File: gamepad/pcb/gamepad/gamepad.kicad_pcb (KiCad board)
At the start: 2 copper layers, 67.8 x 67.8 mm, 10 parts, among them U1 Pico, U2 ADC

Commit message: feat: some pcb stuff
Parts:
- added U3: RP2040-ZERO, RP2040-ZERO:MODULE_RP2040-ZERO, F.Cu at (145.9, 70.3)

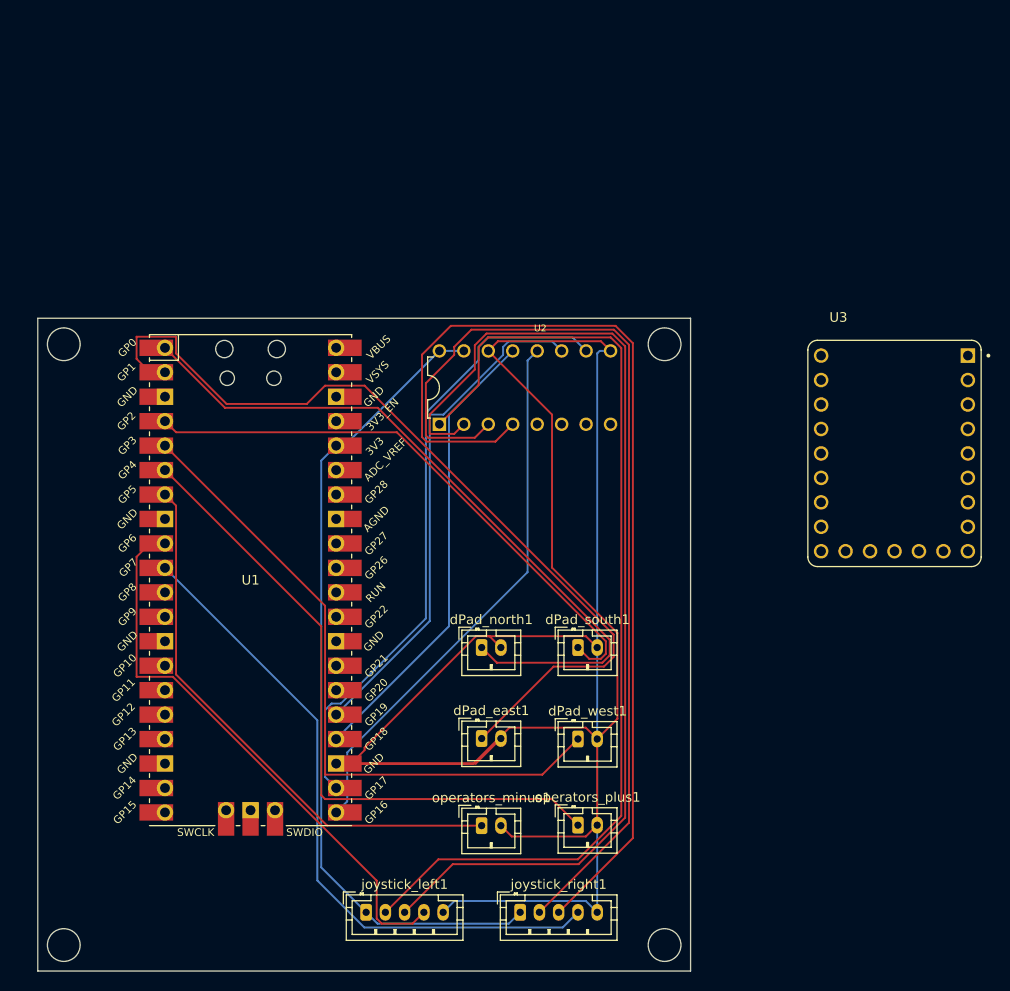
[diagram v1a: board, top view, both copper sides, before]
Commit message: upt: pico to waveshare zero
change out the pcb to have a waveshare zero instead of a pico
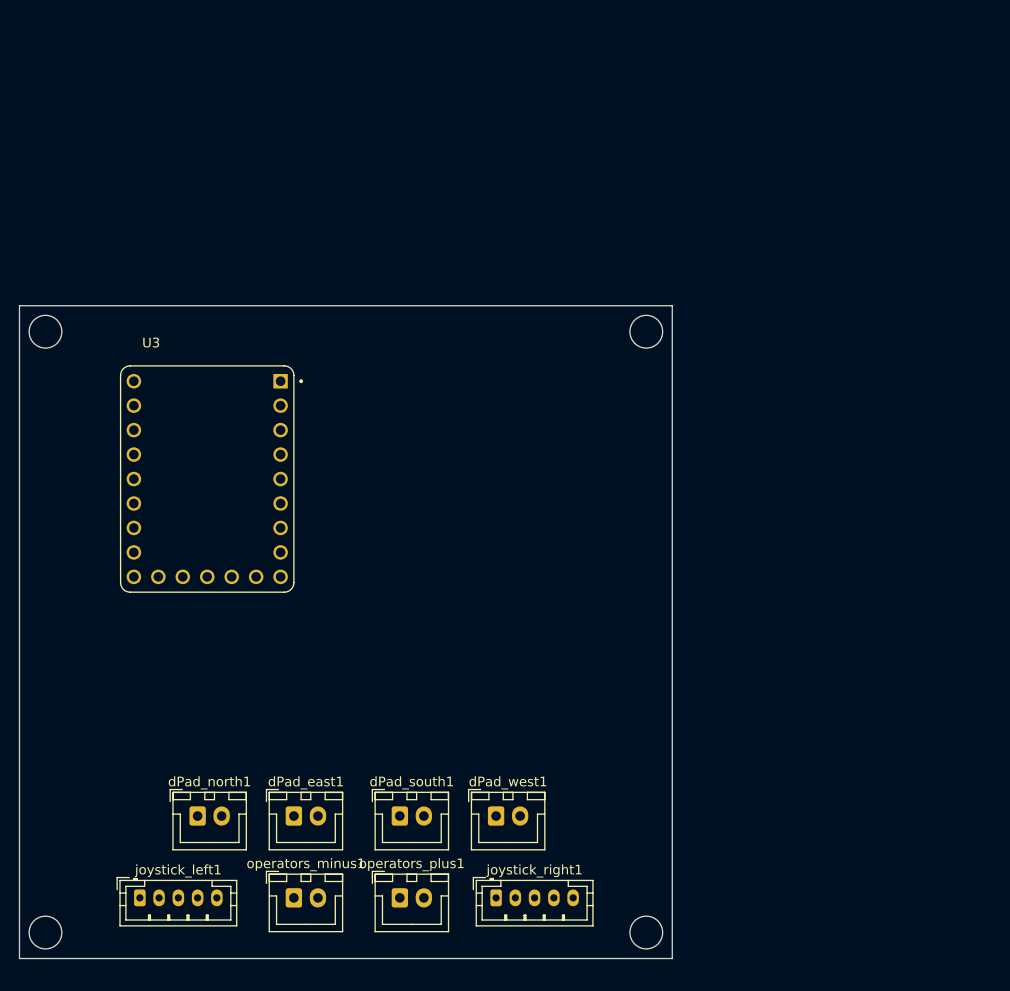
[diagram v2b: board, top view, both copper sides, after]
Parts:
- removed U1: Pico, MCU_RaspberryPi_and_Boards:RPi_Pico_SMD_TH
- removed U2: ADC, MCU-MCP3008:DIP16-2.54-19.2X7.62MM
- dPad_east1, dPad_north1, dPad_south1, dPad_west1, operators_minus1, operators_plus1: footprint Connector_JST:JST_PH_B2B-PH-K_1x02_P2.00mm_Vertical -> Connector_JST:JST_XH_B2B-XH-A_1x02_P2.50mm_Vertical
- moved U3 71.4 mm to (74.5, 73.0)
- moved dPad_north1 34.3 mm to (73.5, 108.0)
- moved dPad_south1 25.5 mm to (94.5, 108.0)
- moved joystick_left1 23.5 mm to (67.5, 116.5)
- moved dPad_east1 21.1 mm to (83.5, 108.0)
- moved operators_minus1 20.9 mm to (83.5, 116.5)
- moved operators_plus1 20.0 mm to (94.5, 116.5)
- moved dPad_west1 11.7 mm to (104.5, 108.0)
- moved joystick_right1 2.92 mm to (104.5, 116.5)
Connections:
- U3 pad 1: unconnected-(U3-GP0-Pad1) -> Net-(U3-GP0)
- U3 pad 17: unconnected-(U3-GP26-Pad17) -> Net-(U3-GP26)
- U3 pad 18: unconnected-(U3-GP27-Pad18) -> Net-(U3-GP27)
- U3 pad 19: unconnected-(U3-GP28-Pad19) -> Net-(U3-GP28)
- U3 pad 2: unconnected-(U3-GP1-Pad2) -> Net-(U3-GP1)
- U3 pad 20: unconnected-(U3-GP29-Pad20) -> Net-(U3-GP29)
- U3 pad 21: unconnected-(U3-3V3-Pad21) -> +3V3
- U3 pad 22: unconnected-(U3-GND-Pad22) -> GND
- U3 pad 3: unconnected-(U3-GP2-Pad3) -> Net-(U3-GP2)
- U3 pad 4: unconnected-(U3-GP3-Pad4) -> Net-(U3-GP3)
- U3 pad 5: unconnected-(U3-GP4-Pad5) -> Net-(U3-GP4)
- U3 pad 6: unconnected-(U3-GP5-Pad6) -> Net-(U3-GP5)
- U3 pad 7: unconnected-(U3-GP6-Pad7) -> Net-(U3-GP6)
- U3 pad 8: unconnected-(U3-GP7-Pad8) -> Net-(U3-GP7)
- dPad_east1 pad 1: Net-(U1-GPIO1) -> Net-(U3-GP1)
- dPad_north1 pad 1: Net-(U1-GPIO0) -> Net-(U3-GP0)
- dPad_south1 pad 1: Net-(U1-GPIO2) -> Net-(U3-GP2)
- dPad_west1 pad 1: Net-(U1-GPIO3) -> Net-(U3-GP3)
- joystick_left1 pad 2: Net-(U2-CH0) -> Net-(U3-GP26)
- joystick_left1 pad 3: Net-(U2-CH1) -> Net-(U3-GP27)
- joystick_left1 pad 4: Net-(U1-GPIO6) -> Net-(U3-GP6)
- joystick_right1 pad 2: Net-(U2-CH2) -> Net-(U3-GP28)
- joystick_right1 pad 3: Net-(U2-CH3) -> Net-(U3-GP29)
- joystick_right1 pad 4: Net-(U1-GPIO7) -> Net-(U3-GP7)
- operators_minus1 pad 1: Net-(U1-GPIO5) -> Net-(U3-GP5)
- operators_plus1 pad 1: Net-(U1-GPIO4) -> Net-(U3-GP4)
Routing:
- net GND: track 239.2 -> 0.00 mm
- net Net-(U2-CH1): track 107.7 -> 0.00 mm
- net Net-(U2-CH3): track 105.1 -> 0.00 mm
- net Net-(U2-CH0): track 102.7 -> 0.00 mm
- net Net-(U2-CH2): track 99.9 -> 0.00 mm
- net Net-(U1-GPIO1): track 90.3 -> 0.00 mm
- net +3V3: track 85.4 -> 0.00 mm
- net Net-(U1-GPIO0): track 76.2 -> 0.00 mm
- net Net-(U1-GPIO3): track 68.9 -> 0.00 mm
- net Net-(U1-GPIO7): track 68.8 -> 0.00 mm
- net Net-(U1-GPIO4): track 68.4 -> 0.00 mm
- net Net-(U1-GPIO17): track 65.6 -> 0.00 mm
- net Net-(U1-GPIO2): track 60.2 -> 0.00 mm
- net Net-(U1-GPIO6): track 59.2 -> 0.00 mm
- net Net-(U1-GPIO5): track 57.4 -> 0.00 mm
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
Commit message: upt: pcb
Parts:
- added cardinal_down1: Conn_01x02, Connector_JST:JST_XH_B2B-XH-A_1x02_P2.50mm_Vertical, F.Cu at (81.0, 55.0)
- added cardinal_left1: Conn_01x02, Connector_JST:JST_XH_B2B-XH-A_1x02_P2.50mm_Vertical, F.Cu at (81.0, 46.0)
- added cardinal_right1: Conn_01x02, Connector_JST:JST_XH_B2B-XH-A_1x02_P2.50mm_Vertical, F.Cu at (81.0, 64.0)
- added cardinal_up1: Conn_01x02, Connector_JST:JST_XH_B2B-XH-A_1x02_P2.50mm_Vertical, F.Cu at (81.0, 73.0)
- moved operators_plus1 88.4 mm to (127.5, 34.5), turned to -90 degrees
- moved operators_minus1 79.5 mm to (81.0, 37.0), turned to 90 degrees
- moved dPad_west1 68.5 mm to (127.5, 43.5), turned to -90 degrees
- moved dPad_north1 65.6 mm to (127.5, 70.8), turned to -90 degrees
- moved dPad_south1 64.6 mm to (127.5, 52.5), turned to -90 degrees
- moved dPad_east1 64.0 mm to (127.5, 61.5), turned to -90 degrees
- moved joystick_right1 43.6 mm to (127.5, 79.5), turned to -90 degrees
- moved joystick_left1 32.2 mm to (81.0, 87.3), turned to 90 degrees
- moved U3 31.2 mm to (105.5, 76.3), turned to 180 degrees
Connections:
- U3 pad 10: unconnected-(U3-GP9-Pad10) -> Net-(U3-GP9)
- U3 pad 11: unconnected-(U3-GP10-Pad11) -> Net-(U3-GP10)
- U3 pad 12: unconnected-(U3-GP11-Pad12) -> Net-(U3-GP11)
- U3 pad 9: unconnected-(U3-GP8-Pad9) -> Net-(U3-GP8)
- joystick_left1 pad 4: Net-(U3-GP6) -> Net-(U3-GP10)
- joystick_right1 pad 4: Net-(U3-GP7) -> Net-(U3-GP11)
- operators_minus1 pad 1: Net-(U3-GP5) -> Net-(U3-GP9)
- operators_plus1 pad 1: Net-(U3-GP4) -> Net-(U3-GP8)
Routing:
- net GND: track 0.00 -> 242.4 mm
- net Net-(U3-GP11): track 0.00 -> 101.6 mm
- net Net-(U3-GP28): track 0.00 -> 89.5 mm
- net +3V3: track 0.00 -> 50.3 mm
- net Net-(U3-GP3): track 0.00 -> 48.1 mm
- net Net-(U3-GP8): track 0.00 -> 47.1 mm
- net Net-(U3-GP27): track 0.00 -> 42.3 mm
- net Net-(U3-GP2): track 0.00 -> 42.2 mm
- net Net-(U3-GP1): track 0.00 -> 38.8 mm
- net Net-(U3-GP26): track 0.00 -> 38.1 mm
- net Net-(U3-GP9): track 0.00 -> 37.2 mm
- net Net-(U3-GP0): track 0.00 -> 36.1 mm
- net Net-(U3-GP10): track 0.00 -> 32.1 mm
- net Net-(U3-GP7): track 0.00 -> 29.7 mm
- net Net-(U3-GP6): track 0.00 -> 23.6 mm
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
